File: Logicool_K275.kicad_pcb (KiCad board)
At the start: 2 copper layers, 52 x 25 mm, 33 parts, among them IC1 RP2040_QFN56, J1 Conn_01x05, J2 Conn_01x24, SW3 SW_Push, SW4 SW_Push, U3 24LC1025, U4 AP2112K-3.3, U5 W25Q32JVSS, Y1 Crystal

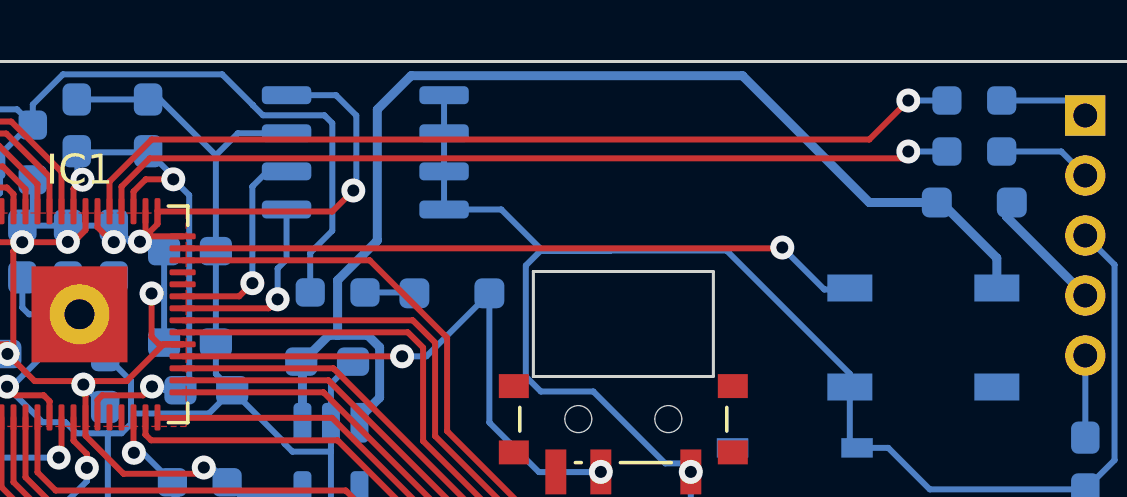
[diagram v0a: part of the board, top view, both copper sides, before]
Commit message: Neopixelの信号線にレベル変換を追加
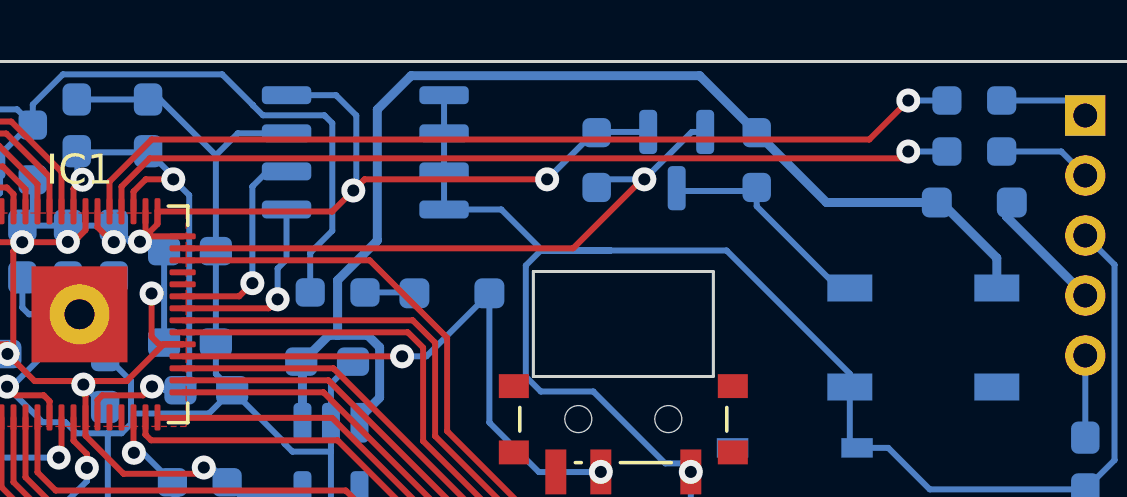
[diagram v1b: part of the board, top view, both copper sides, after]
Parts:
- added Q1: BSS138, Package_TO_SOT_SMD:SOT-23, B.Cu at (136.8, 129.3)
- added R7: 4.7k, Resistor_SMD:R_0603_1608Metric_Pad0.98x0.95mm_HandSolder, B.Cu at (134.1, 129.3)
- added R8: 4.7k, Resistor_SMD:R_0603_1608Metric_Pad0.98x0.95mm_HandSolder, B.Cu at (139.4, 129.3)
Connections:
- D1 pad 4: LED -> LED_5V
- IC1 pad 41: LED -> LED_3V3
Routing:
- net LED: track 22.8 -> 0.00 mm, vias 1 -> 0
- net LED_3V3: track 0.00 -> 20.7 mm, vias 0 -> 1
- net +3.3V: track 70.1 -> 80.7 mm, vias 10 -> 11
- net LED_5V: track 0.00 -> 7.63 mm
